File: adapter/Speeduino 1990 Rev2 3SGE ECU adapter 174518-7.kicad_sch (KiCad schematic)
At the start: 17 parts, among them J1 Conn_02x20_Odd_Even, J2 Screw_Terminal_01x02, P1 CONN_3, P10 CONN_8, P11 CONN_8, P12 CONN_8, P13 CONN_8, P2 CONN_3, P3 Conn_01x04_Male, P4 CONN_1, P5 CONN_1, P6 Conn_01x04_Male, P7 174518-7, P8 CONN_8, P9 CONN_8

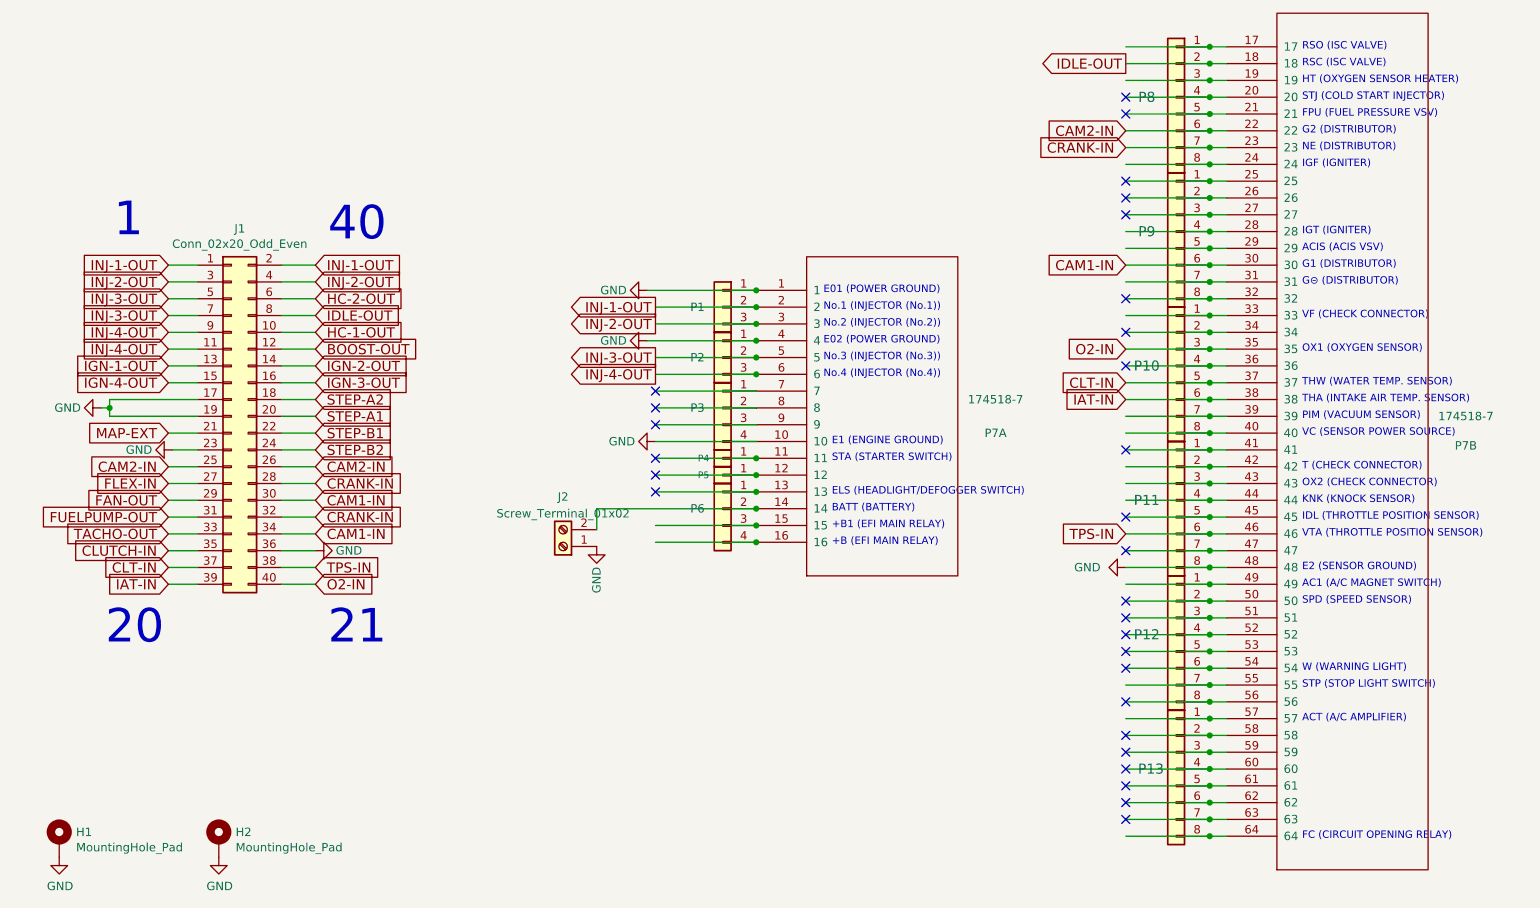
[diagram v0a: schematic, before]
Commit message: Finished adapter board, slight changes to ECU
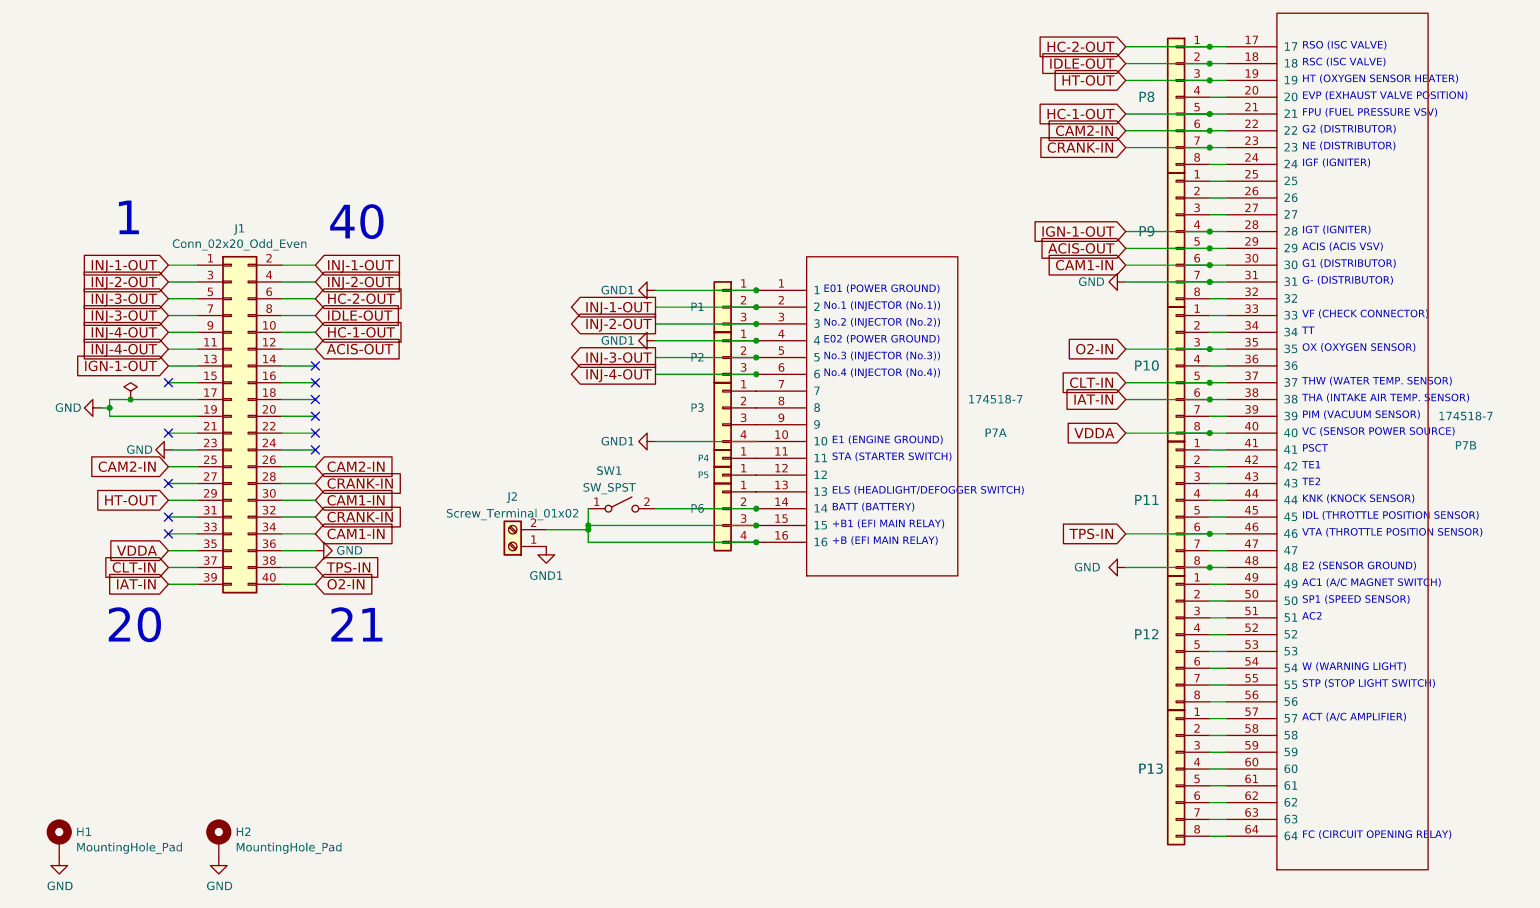
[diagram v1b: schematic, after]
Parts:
- added SW1: SW_SPST, Jumper:SolderJumper-2_P1.3mm_Bridged_Pad1.0x1.5mm, symbol Switch:SW_SPST
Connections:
- net BOOST-OUT is gone; now on net ACIS-OUT: J1.12 (Pin_12)
- net CLUTCH-IN is gone; now on net VDDA: J1.35 (Pin_35)
- net FAN-OUT is gone; now on net HT-OUT: J1.29 (Pin_29)
- net GND: now also P7.31, P9.7 (Pin_7); no longer J2.1 (Pin_1), P1.1 (Pin_1), P2.1 (Pin_1), P3.4 (Pin_4), P7.1, P7.10, P7.4
- net HC-1-OUT: now also P7.21, P8.5 (Pin_5)
- net HC-2-OUT: now also P7.17, P8.1 (Pin_1)
- net IGN-1-OUT: now also P7.28, P9.4 (Pin_4)
- net at P6.2 (Pin_2), P7.14: now also SW1.2 (B); no longer J2.2 (Pin_2)
- net at P6.3 (Pin_3), P7.15: now also J2.2 (Pin_2), P6.4 (Pin_4), P7.16, SW1.1 (A)
- net HT-OUT: now reaches P7.19, P8.3 (Pin_3)
- net ACIS-OUT: now reaches P7.29, P9.5 (Pin_5)
- net VDDA: now reaches P10.8 (Pin_8), P7.40
- net FLEX-IN: no longer names the net of J1.27 (Pin_27)
- net FUELPUMP-OUT: no longer names the net of J1.31 (Pin_31)
- net IGN-2-OUT: no longer names the net of J1.14 (Pin_14)
- net IGN-3-OUT: no longer names the net of J1.16 (Pin_16)
- net IGN-4-OUT: no longer names the net of J1.15 (Pin_15)
- net MAP-EXT: no longer names the net of J1.21 (Pin_21)
- net STEP-A1: no longer names the net of J1.20 (Pin_20)
- net STEP-A2: no longer names the net of J1.18 (Pin_18)
- net STEP-B1: no longer names the net of J1.22 (Pin_22)
- net STEP-B2: no longer names the net of J1.24 (Pin_24)
- net TACHO-OUT: no longer names the net of J1.33 (Pin_33)
- new net GND1: J2.1 (Pin_1), P1.1 (Pin_1), P2.1 (Pin_1), P3.4 (Pin_4), P7.1, P7.10, P7.4
- no-connect marks 29 -> 11
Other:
- note added: "AC2"
- note added: "EVP (EXHAUST VALVE POSITION)"
- note added: "G- (DISTRIBUTOR)"
- note added: "OX (OXYGEN SENSOR)"
- note added: "PSCT"
- note added: "SP1 (SPEED SENSOR)"
- note added: "TE1"
- note added: "TE2"
- note added: "TT"
- note removed: "G⊝ (DISTRIBUTOR)"
- note removed: "OX1 (OXYGEN SENSOR)"
- note removed: "OX2 (CHECK CONNECTOR)"
- note removed: "SPD (SPEED SENSOR)"
- note removed: "STJ (COLD START INJECTOR)"
- note removed: "T (CHECK CONNECTOR)"
- moved on the sheet: J2
